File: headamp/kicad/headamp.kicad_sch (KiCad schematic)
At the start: 91 parts, among them J1 MAINS 230V, J401 IN L (RCA), J402 IN R (RCA), J403 jack 6,3mm TRS (DT 770 M 80R), K1 9V, SW1 ON/OFF, SW2 S2 wokal, SW202 S2 wokal (P), SW401 S1 crossfeed, T1 OPT SE 5k:80R (>=25H, 45mA), T201 OPT SE 5k:80R (>=25H, 45mA), T301 EI84 100VA: 230V : 250V/0,15A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, U1 ECC82, U2 EL84 (trioda), U202 EL84 (trioda), U301 LD1085 (LDO)

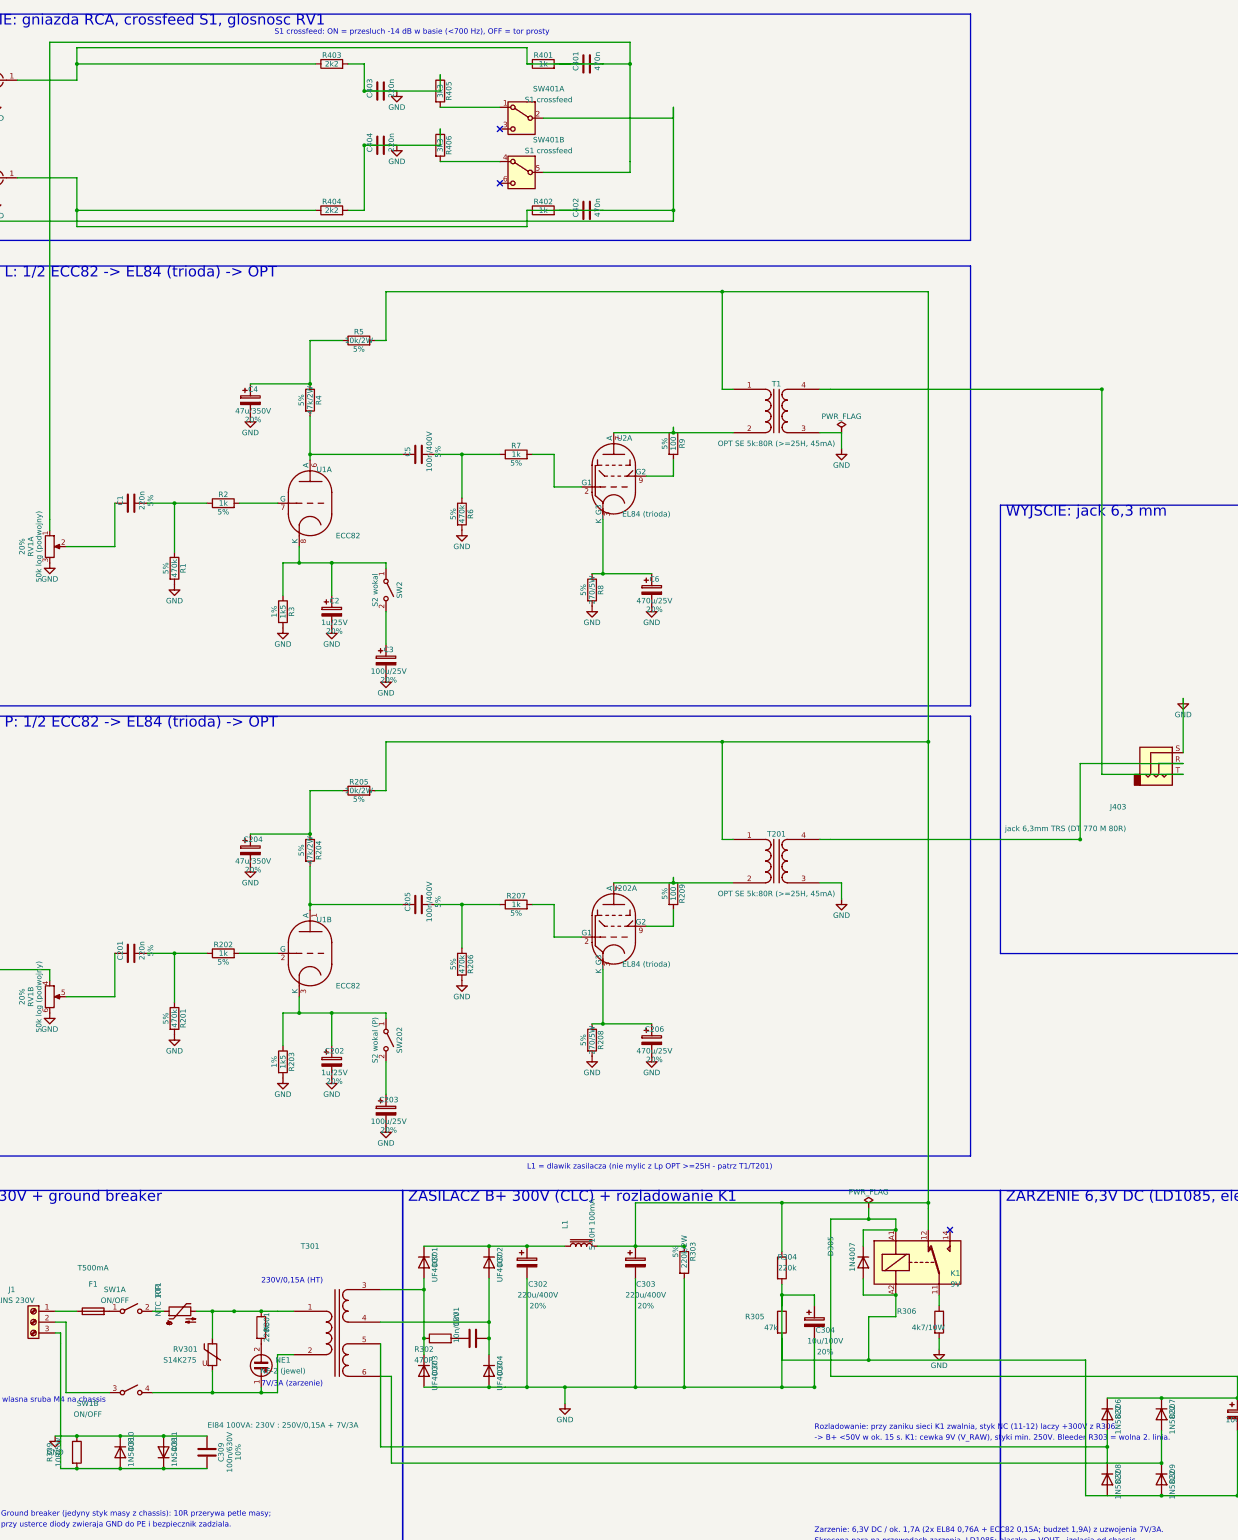
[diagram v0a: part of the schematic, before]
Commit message: headamp: plik roboczy headamp/kicad odtworzony z naprawionego gen.py; .history/ w .gitignore
Poprzednia kopia po zapisie w Eeschema tracila 7 polaczen (nakladajace
sie druty scalane przez KiCad). Netlista 58 sieci, ERC 0/0. Plik .kicad_pro
w postaci zapisanej przez KiCad 10.

Co-Authored-By: Claude Fable 5.1 <noreply@anthropic.com>
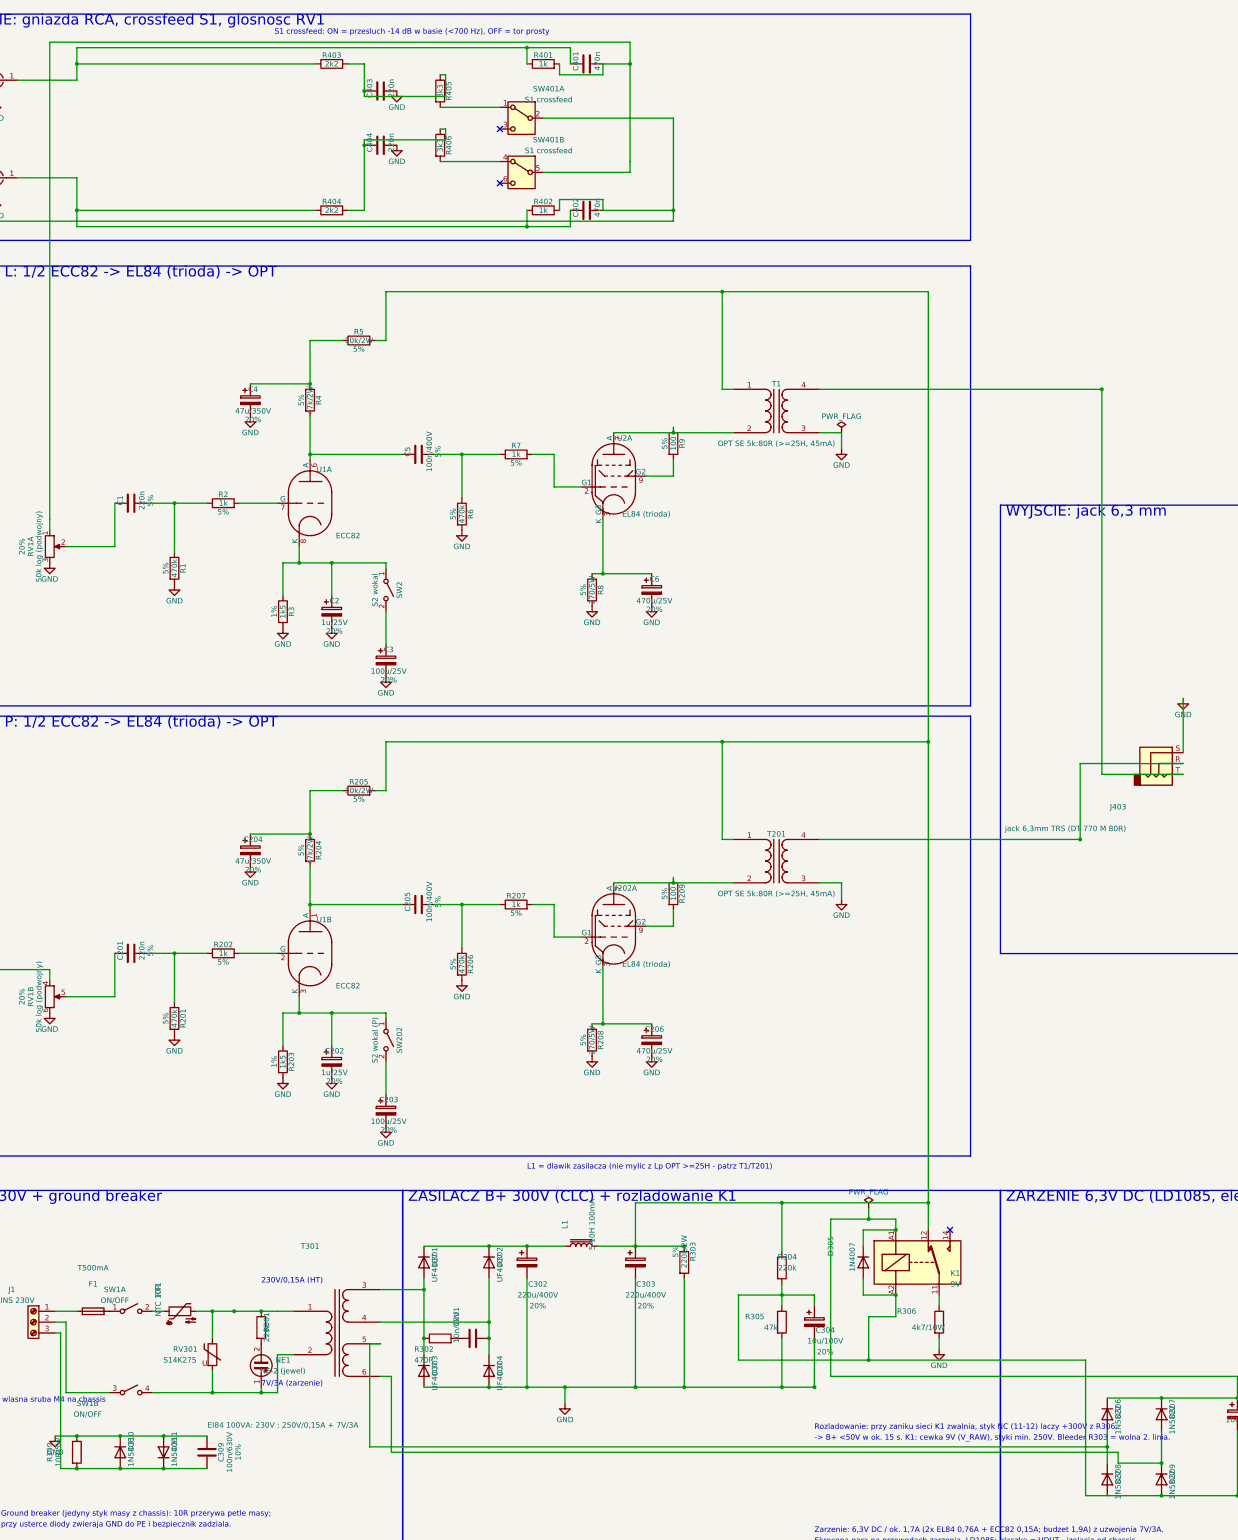
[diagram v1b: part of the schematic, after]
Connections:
- net GND: no longer C304.1, C305.2, C306.2, C307.2, C308.2, D305.2 (A), D308.2 (A), D309.2 (A), K1.A2, R304.2, R305.1, R308.2, U1.9 (F2), U2.5 (F2), U202.5 (F2)
- net at C402.2, R402.2, RV1.4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: no longer C402.1, J402.1 (In), R402.1, R404.1
- net at C401.2, R401.2, RV1.1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: no longer C401.1, J401.1 (In), R401.1, R403.1
- new net: C304.1, C305.2, C306.2, C307.2, C308.2, D305.2 (A), D308.2 (A), D309.2 (A), K1.A2, R304.2, R305.1, R308.2, U1.9 (F2), U2.5 (F2), U202.5 (F2)
- new net: C401.1, J401.1 (In), R401.1, R403.1
- new net: C402.1, J402.1 (In), R402.1, R404.1
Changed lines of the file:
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@@
   (junction (at 185.42 218.44) (diameter 0))
   (junction (at 196.85 185.42) (diameter 0))
+  (junction (at 151.13 22.86) (diameter 0))
   (junction (at 45.72 26.67) (diameter 0))
+  (junction (at 151.13 64.77) (diameter 0))
   (junction (at 45.72 60.96) (diameter 0))
   (junction (at 175.26 26.67) (diameter 0))
@@
   (wire (pts (xy 45.72 26.67) (xy 101.6 26.67)) (stroke (width 0) (type default)))
   (wire (pts (xy 45.72 26.67) (xy 45.72 22.86)) (stroke (width 0) (type default)))
-  (wire (pts (xy 45.72 22.86) (xy 151.13 22.86)) (stroke (width 0) (type default)))
+  (wire (pts (xy 45.72 22.86) (xy 161.29 22.86)) (stroke (width 0) (type default)))
   (wire (pts (xy 151.13 22.86) (xy 151.13 26.67)) (stroke (width 0) (type default)))
+  (wire (pts (xy 161.29 22.86) (xy 161.29 26.67)) (stroke (width 0) (type default)))
   (wire (pts (xy 31.75 53.34) (xy 45.72 53.34)) (stroke (width 0) (type default)))
   (wire (pts (xy 45.72 53.34) (xy 45.72 60.96)) (stroke (width 0) (type default)))
   (wire (pts (xy 45.72 60.96) (xy 101.6 60.96)) (stroke (width 0) (type default)))
   (wire (pts (xy 45.72 60.96) (xy 45.72 64.77)) (stroke (width 0) (type default)))
-  (wire (pts (xy 45.72 64.77) (xy 151.13 64.77)) (stroke (width 0) (type default)))
+  (wire (pts (xy 45.72 64.77) (xy 161.29 64.77)) (stroke (width 0) (type default)))
   (wire (pts (xy 151.13 64.77) (xy 151.13 60.96)) (stroke (width 0) (type default)))
-  (wire (pts (xy 151.13 26.67) (xy 161.29 26.67)) (stroke (width 0) (type default)))
-  (wire (pts (xy 158.75 26.67) (xy 168.91 26.67)) (stroke (width 0) (type default)))
-  (wire (pts (xy 151.13 60.96) (xy 161.29 60.96)) (stroke (width 0) (type default)))
-  (wire (pts (xy 158.75 60.96) (xy 168.91 60.96)) (stroke (width 0) (type default)))
+  (wire (pts (xy 161.29 64.77) (xy 161.29 60.96)) (stroke (width 0) (type default)))
+  (wire (pts (xy 158.75 26.67) (xy 158.75 29.21)) (stroke (width 0) (type default)))
+  (wire (pts (xy 158.75 29.21) (xy 168.91 29.21)) (stroke (width 0) (type default)))
+  (wire (pts (xy 168.91 29.21) (xy 168.91 26.67)) (stroke (width 0) (type default)))
+  (wire (pts (xy 158.75 60.96) (xy 158.75 58.42)) (stroke (width 0) (type default)))
+  (wire (pts (xy 158.75 58.42) (xy 168.91 58.42)) (stroke (width 0) (type default)))
+  (wire (pts (xy 168.91 58.42) (xy 168.91 60.96)) (stroke (width 0) (type default)))
   (wire (pts (xy 168.91 26.67) (xy 175.26 26.67)) (stroke (width 0) (type default)))
   (wire (pts (xy 175.26 21.59) (xy 175.26 49.53)) (stroke (width 0) (type default)))
@@
   (wire (pts (xy 39.37 21.59) (xy 39.37 133.35)) (stroke (width 0) (type default)))
   (wire (pts (xy 168.91 60.96) (xy 185.42 60.96)) (stroke (width 0) (type default)))
-  (wire (pts (xy 185.42 36.83) (xy 185.42 63.5)) (stroke (width 0) (type default)))
+  (wire (pts (xy 185.42 39.37) (xy 185.42 63.5)) (stroke (width 0) (type default)))
   (wire (pts (xy 185.42 63.5) (xy 20.32 63.5)) (stroke (width 0) (type default)))
   (wire (pts (xy 20.32 63.5) (xy 20.32 238.76)) (stroke (width 0) (type default)))
@@
   (wire (pts (xy 109.22 26.67) (xy 113.03 26.67)) (stroke (width 0) (type default)))
   (wire (pts (xy 113.03 26.67) (xy 113.03 33.02)) (stroke (width 0) (type default)))
-  (wire (pts (xy 113.03 33.02) (xy 130.81 33.02)) (stroke (width 0) (type default)))
-  (wire (pts (xy 130.81 33.02) (xy 130.81 29.21)) (stroke (width 0) (type default)))
+  (wire (pts (xy 113.03 33.02) (xy 113.03 34.29)) (stroke (width 0) (type default)))
+  (wire (pts (xy 113.03 34.29) (xy 132.08 34.29)) (stroke (width 0) (type default)))
+  (wire (pts (xy 132.08 34.29) (xy 132.08 29.21)) (stroke (width 0) (type default)))
+  (wire (pts (xy 132.08 29.21) (xy 130.81 29.21)) (stroke (width 0) (type default)))
   (wire (pts (xy 130.81 36.83) (xy 144.78 36.83)) (stroke (width 0) (type default)))
   (wire (pts (xy 154.94 39.37) (xy 185.42 39.37)) (stroke (width 0) (type default)))
-  (wire (pts (xy 185.42 39.37) (xy 185.42 36.83)) (stroke (width 0) (type default)))
   (wire (pts (xy 109.22 60.96) (xy 113.03 60.96)) (stroke (width 0) (type default)))
   (wire (pts (xy 113.03 60.96) (xy 113.03 45.72)) (stroke (width 0) (type default)))
-  (wire (pts (xy 113.03 45.72) (xy 130.81 45.72)) (stroke (width 0) (type default)))
-  (wire (pts (xy 130.81 45.72) (xy 130.81 41.91)) (stroke (width 0) (type default)))
+  (wire (pts (xy 113.03 45.72) (xy 113.03 44.45)) (stroke (width 0) (type default)))
+  (wire (pts (xy 113.03 44.45) (xy 132.08 44.45)) (stroke (width 0) (type default)))
+  (wire (pts (xy 132.08 44.45) (xy 132.08 41.91)) (stroke (width 0) (type default)))
+  (wire (pts (xy 132.08 41.91) (xy 130.81 41.91)) (stroke (width 0) (type default)))
   (wire (pts (xy 130.81 49.53) (xy 144.78 49.53)) (stroke (width 0) (type default)))
   (wire (pts (xy 154.94 52.07) (xy 175.26 52.07)) (stroke (width 0) (type default)))
@@
   (wire (pts (xy 245.11 185.42) (xy 245.11 293.37)) (stroke (width 0) (type default)))
   (wire (pts (xy 287.02 346.71) (xy 287.02 354.33)) (stroke (width 0) (type default)))
-  (wire (pts (xy 116.84 326.39) (xy 116.84 350.52)) (stroke (width 0) (type default)))
-  (wire (pts (xy 116.84 350.52) (xy 287.02 350.52)) (stroke (width 0) (type default)))
+  (wire (pts (xy 116.84 326.39) (xy 114.3 326.39)) (stroke (width 0) (type default)))
+  (wire (pts (xy 114.3 326.39) (xy 114.3 350.52)) (stroke (width 0) (type default)))
+  (wire (pts (xy 114.3 350.52) (xy 287.02 350.52)) (stroke (width 0) (type default)))
   (wire (pts (xy 299.72 346.71) (xy 299.72 354.33)) (stroke (width 0) (type default)))
   (wire (pts (xy 116.84 334.01) (xy 119.38 334.01)) (stroke (width 0) (type default)))
-  (wire (pts (xy 119.38 334.01) (xy 119.38 354.33)) (stroke (width 0) (type default)))
-  (wire (pts (xy 119.38 354.33) (xy 299.72 354.33)) (stroke (width 0) (type default)))
+  (wire (pts (xy 119.38 334.01) (xy 119.38 351.79)) (stroke (width 0) (type default)))
+  (wire (pts (xy 119.38 351.79) (xy 289.56 351.79)) (stroke (width 0) (type default)))
+  (wire (pts (xy 289.56 351.79) (xy 289.56 354.33)) (stroke (width 0) (type default)))
+  (wire (pts (xy 289.56 354.33) (xy 299.72 354.33)) (stroke (width 0) (type default)))
   (wire (pts (xy 287.02 339.09) (xy 299.72 339.09)) (stroke (width 0) (type default)))
   (wire (pts (xy 299.72 339.09) (xy 317.5 339.09)) (stroke (width 0) (type default)))
@@
   (wire (pts (xy 287.02 361.95) (xy 281.94 361.95)) (stroke (width 0) (type default)))
   (wire (pts (xy 387.35 361.95) (xy 387.35 364.49)) (stroke (width 0) (type default)))
-  (wire (pts (xy 210.82 314.96) (xy 210.82 330.2)) (stroke (width 0) (type default)))
-  (wire (pts (xy 210.82 330.2) (xy 231.14 330.2)) (stroke (width 0) (type default)))
+  (wire (pts (xy 210.82 314.96) (xy 200.66 314.96)) (stroke (width 0) (type default)))
+  (wire (pts (xy 200.66 314.96) (xy 200.66 330.2)) (stroke (width 0) (type default)))
+  (wire (pts (xy 200.66 330.2) (xy 231.14 330.2)) (stroke (width 0) (type default)))
   (wire (pts (xy 231.14 320.04) (xy 231.14 330.2)) (stroke (width 0) (type default)))
   (wire (pts (xy 231.14 330.2) (xy 281.94 330.2)) (stroke (width 0) (type default)))
